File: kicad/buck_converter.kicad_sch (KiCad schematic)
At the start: 46 parts, among them J5 SolderPad, J6 SolderPad, Q2 CSD19537Q3, Q3 BSZ096N10LS5, U2 LM5146

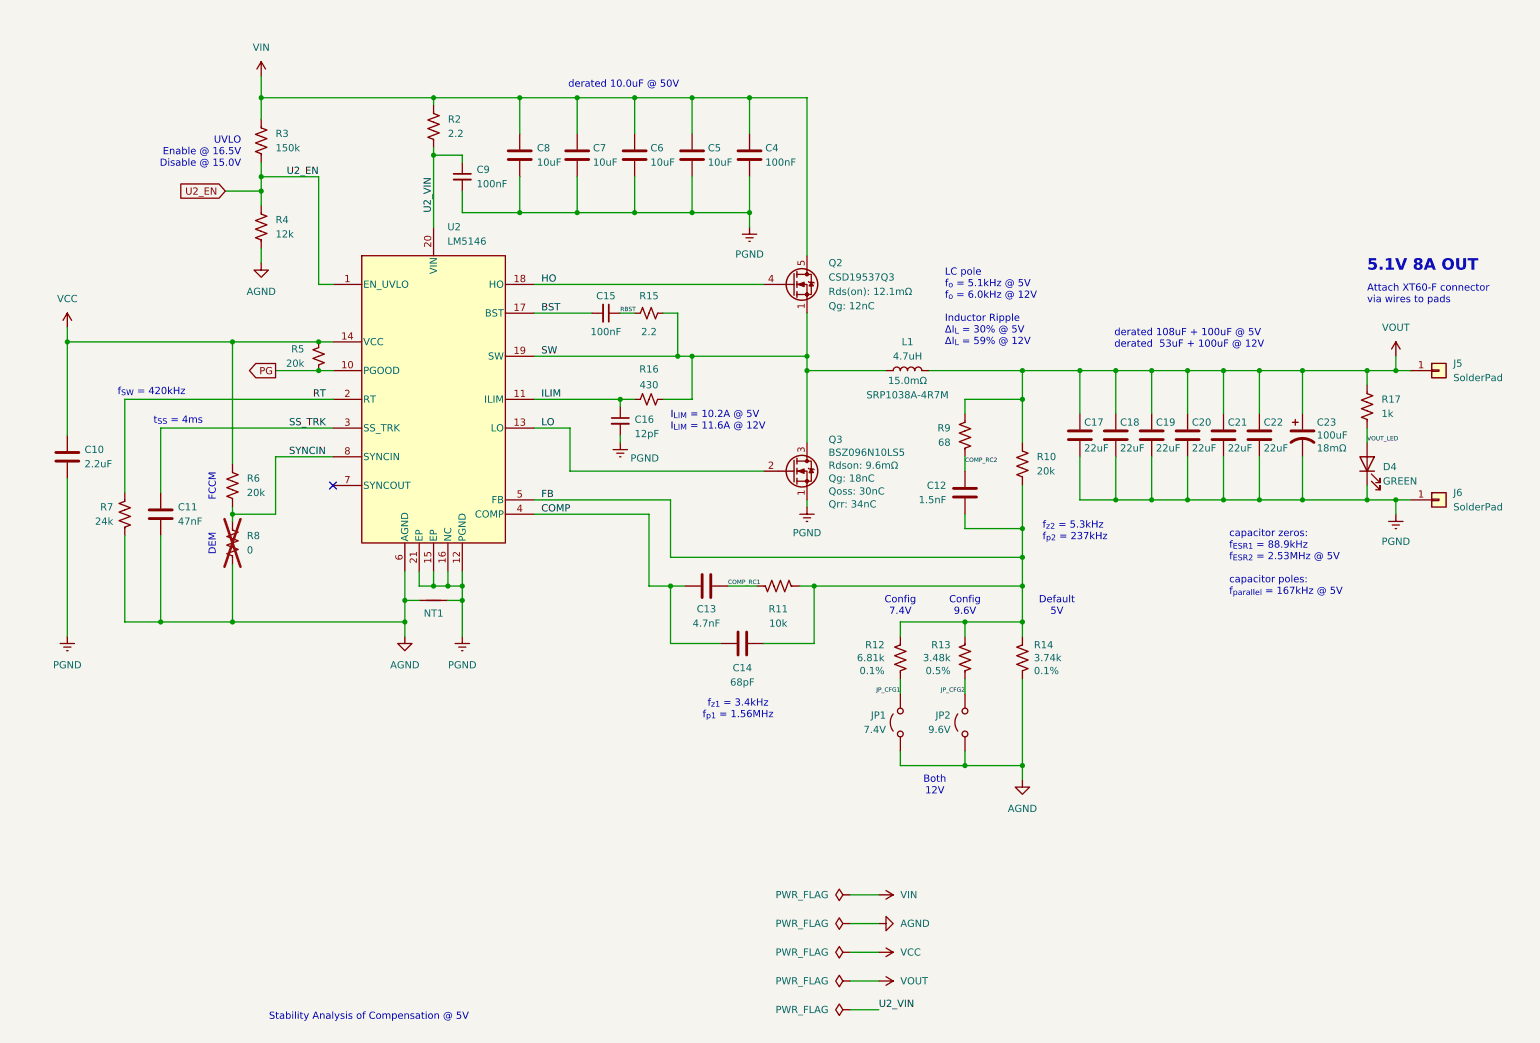
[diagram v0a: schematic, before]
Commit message: Adjusted licensing for club
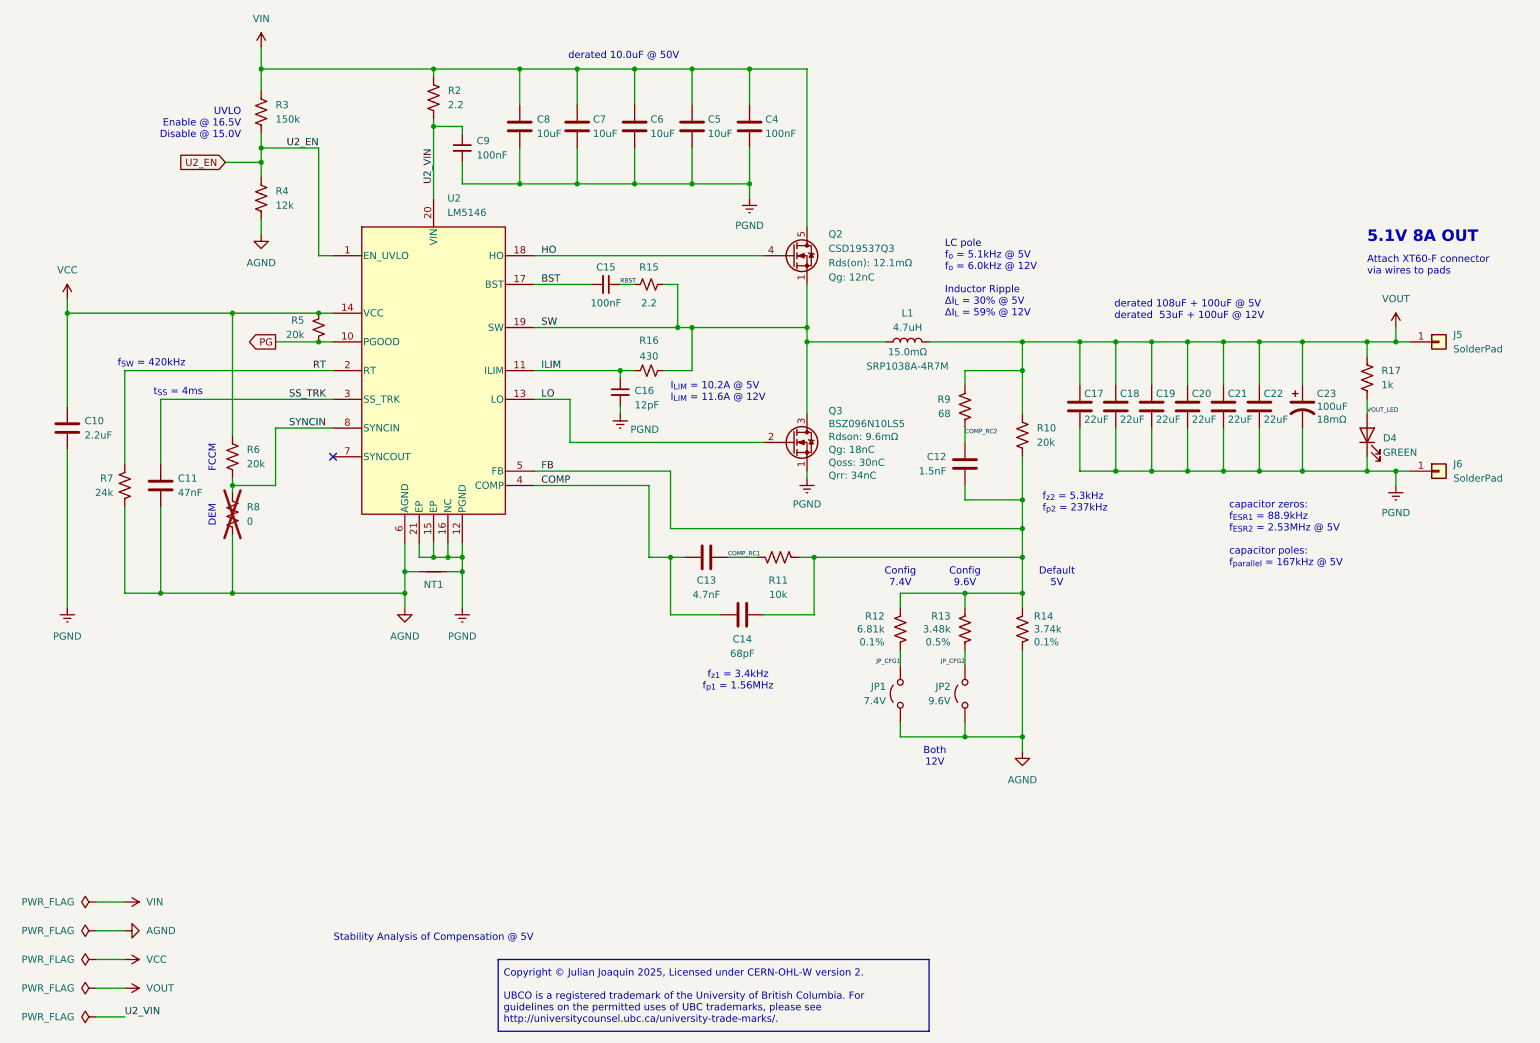
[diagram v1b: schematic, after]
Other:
- company: Author: Julian Joaquin -> UBCO Aerospace Club
- moved on the sheet: C10, C11, C12, C13, C14, C15, C16, C17, C18, C19, C20, C21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
